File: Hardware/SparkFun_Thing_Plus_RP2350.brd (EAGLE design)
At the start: 22.9 x 58.4 mm, 161 parts, among them J1 THING_PLUS_LOGICAL, J3 QWIIC_RIGHT_ANGLE, J6 MICRO-SD-ATOM, Q1 100mA/20V/3.8Ω, U1 RP2350A, U2 RM2, U3 RT9080-33GJ5, U4 LM66200, U5 W25QXX128MBIT, U6 MCP73831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

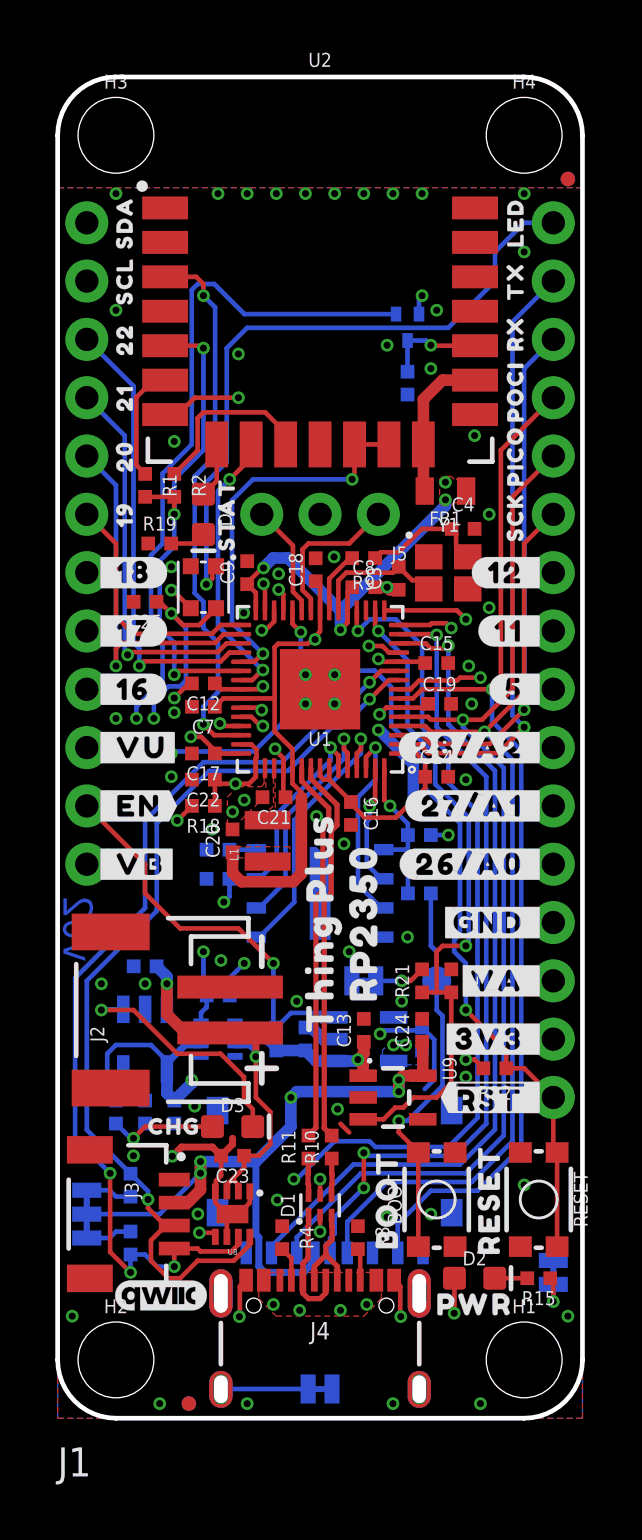
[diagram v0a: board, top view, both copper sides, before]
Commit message: Design review updates
Replace USB ESD diode with larger package for better manufacturing reliability
Add ordering instructions
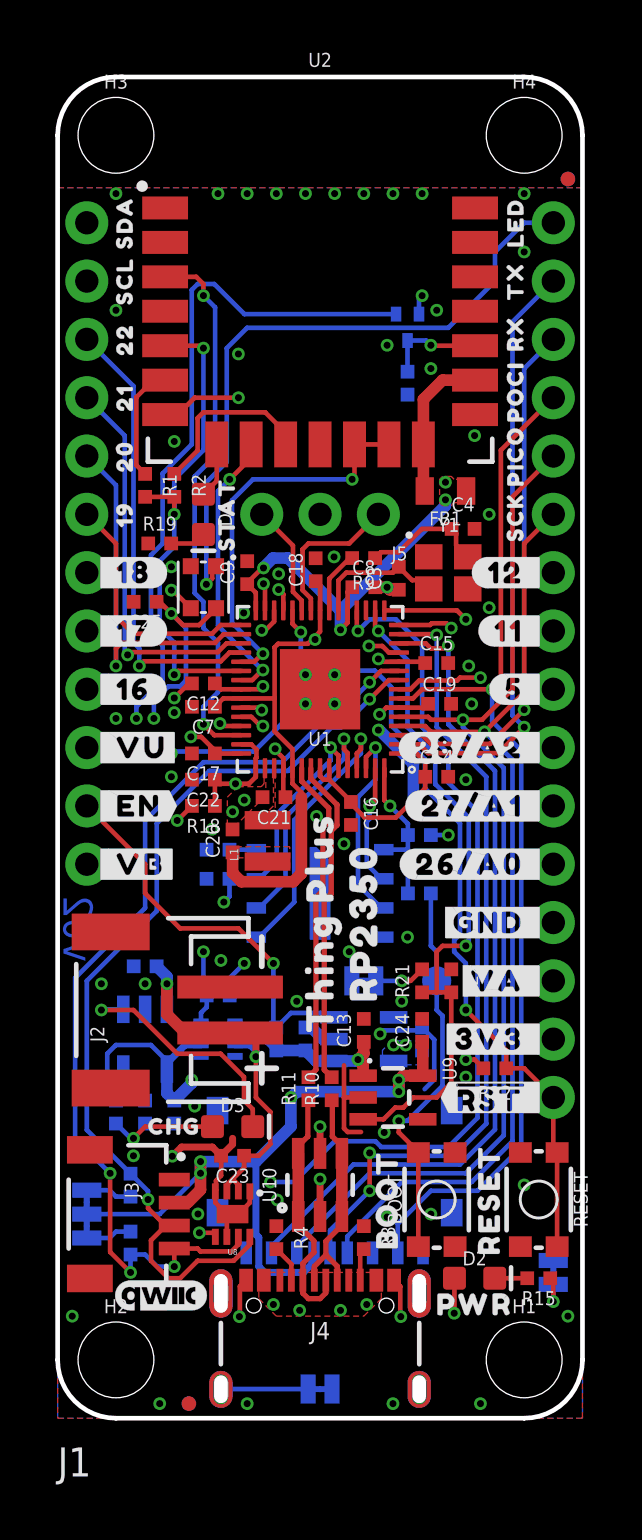
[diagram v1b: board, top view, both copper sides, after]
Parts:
- removed D1: PRTR5V0U2F, SparkFun-IC-Power:SOT886
- added LOGO5: SPECIAL_INSTRUCTIONS-ORDERING, SparkFun-Aesthetics:ORDERING_INSTRUCTIONS
- added U10: ESD Diode, SparkFun-DiscreteSemi:SOT-23-6
- moved FRAME1 14.0 mm to (66.0, -7.62)
- moved R10 2.54 mm to (11.9, 14.4)
- moved R11 2.54 mm to (10.9, 14.4)
- moved R3 0.25 mm to (13.3, 7.87)
- moved R4 0.25 mm to (9.53, 7.87)
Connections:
- removed net N$24: D1.4, R10.1
- removed net N$25: D1.6, R11.1
- net GND: now also U10.2; no longer D1.2
- net N$7: now also R11.1, U10.1, U10.6; no longer D1.1
- net N$8: now also R10.1, U10.3, U10.4; no longer D1.3
- net V_USB: now also U10.5; no longer D1.5
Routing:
- net N$7: track 5.28 -> 10.8 mm
- net N$8: track 4.47 -> 9.83 mm
- net GND: track 35.9 -> 40.7 mm
- net USB_D_P: track 16.8 -> 14.3 mm
- net USB_D_N: track 16.9 -> 14.3 mm
- net N$24: track 1.63 -> 0.00 mm
- net N$25: track 1.63 -> 0.00 mm
- net V_USB: track 48.2 -> 49.4 mm
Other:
- board text added: "4-layer JLC7628 Stackup Material: TG135-140 1oz outer layers 0.5oz inner layers Board thickness: 1.6mm Soldermask: Red Silkscreen: White Surface Finish: Lead-Free HASL"

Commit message: Add PSRAM
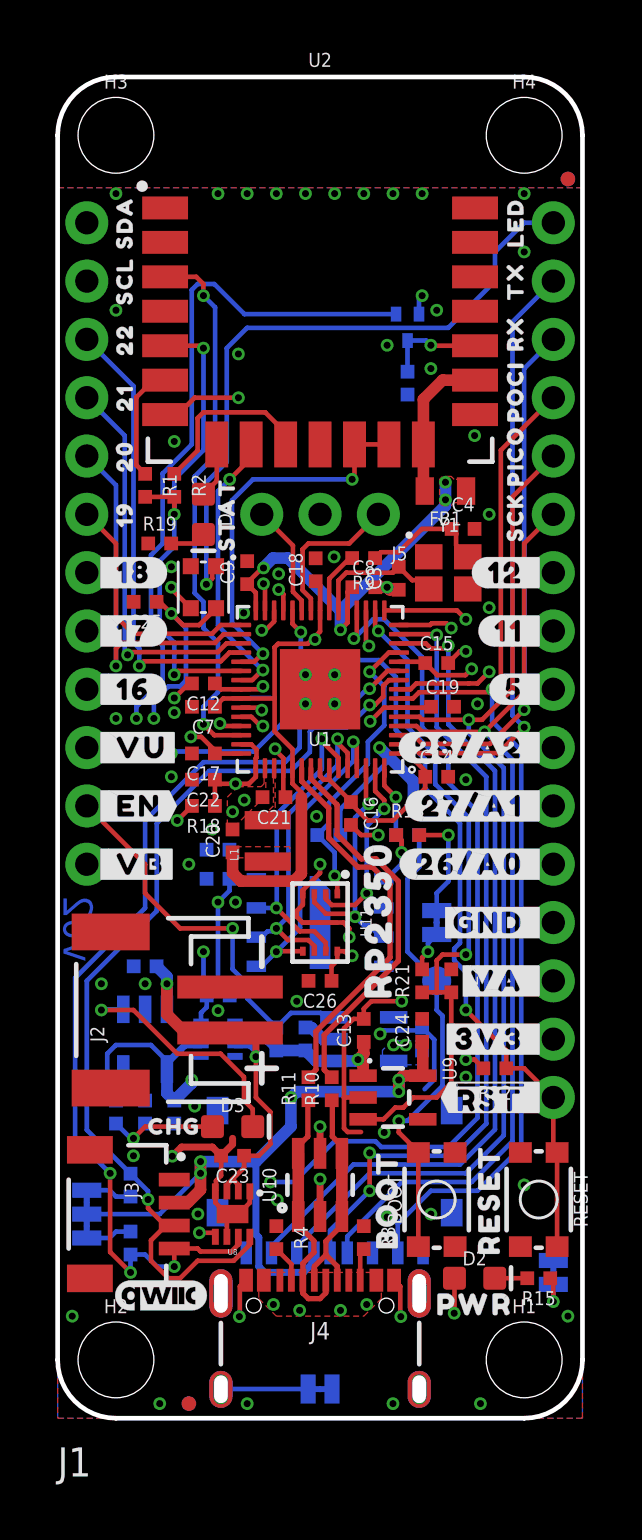
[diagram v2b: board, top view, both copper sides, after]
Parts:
- removed U$37: (no value), output:#_A0#26#0
- added C26: 0.1uF, SparkFun-Capacitors:0402-TIGHT
- added R23: 10k, SparkFun-Resistors:0402-TIGHT
- added U11: APS6404L-3SQR-ZR, RP2350A:APS6404L-3SQR-ZR
- U$16: device output:#_GND#0 -> output:#_A0#0
- U$44: device output:THING_PLUS0 -> output:#_G#0
- moved U$44 9.91 mm to (21.3, 21.6), flipped to the bottom, turned to 0 degrees
- moved U$26 5.32 mm to (16.5, 22.5), turned to 90 degrees
- moved LP 4.07 mm to (16.5, 21.6), turned to 90 degrees
- moved R14 2.59 mm to (15.2, 25.4)
- moved U$16 2.54 mm to (21.3, 24.1)
- moved C10 1.27 mm to (6.99, 24.8)
- moved C11 1.27 mm to (6.99, 23.5)
- moved U5 1.27 mm to (11.4, 21.6)
- moved U$45 0.65 mm to (14.0, 21.7)
- moved R13 0.51 mm to (15.2, 25.4), flipped to the top, turned to 0 degrees
- moved C19 0.18 mm to (16.8, 31.0)
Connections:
- new net PSRAM_!CS!: R23.1, U1.12, U11.1
- net 3.3V: now also C26.1, R23.2, U11.8
- net GND: now also C26.2, U11.4, U11.9
- net LED_IN: now also U1.18; no longer U1.12
- net QSPI_CLK: now also U11.6
- net QSPI_D0: now also U11.5
- net QSPI_D1: now also U11.2
- net QSPI_D2: now also U11.3
- net QSPI_D3: now also U11.7
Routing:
- net PSRAM_!CS!: track 0.00 -> 13.1 mm, vias 0 -> 2
- net 3.3V: track 50.1 -> 63.1 mm, vias 20 -> 19
- net GND: track 40.7 -> 53.4 mm, vias 69 -> 72
- net QSPI_D3: track 8.17 -> 13.8 mm, vias 1 -> 2
- net QSPI_D1: track 5.34 -> 9.27 mm, vias 1 -> 2
- net QSPI_CLK: track 10.4 -> 14.0 mm, vias 1 -> 2
- net !BOOT!: track 17.0 -> 20.1 mm
- net USB_D_P: track 14.3 -> 16.9 mm
- net USB_D_N: track 14.3 -> 16.9 mm
- net QSPI_D0: track 11.9 -> 14.0 mm, vias 1 -> 2
- net QSPI_D2: track 8.90 -> 10.8 mm, vias 1 -> 2
- net SDA: track 71.1 -> 72.2 mm
- net SCL: track 69.8 -> 70.6 mm
- net QSPI_!CS!: track 6.93 -> 6.39 mm, vias 1 -> 2

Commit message: Bump version number to v10
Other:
- board text added: "v10"
- board text removed: "v02"
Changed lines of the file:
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@@
 <wire x1="8.89" y1="20.955" x2="8.89" y2="19.685" width="0.254" layer="21"/>
 <wire x1="8.89" y1="15.875" x2="8.89" y2="14.605" width="0.254" layer="21"/>
-<text x="0.889" y="21.336" size="1.27" layer="16" font="vector" ratio="15" rot="MR270" align="center">v02</text>
+<text x="0.889" y="21.336" size="1.27" layer="16" font="vector" ratio="15" rot="MR270" align="center">v10</text>
 <text x="92.71" y="-7.62" size="1.778" layer="51" font="vector">Dryw Wade</text>
 <dimension x1="5.08" y1="8.89" x2="5.08" y2="0" x3="-1.27" y3="4.445" textsize="1.778" textratio="15" layer="47" unit="inch"/>
@@
 <element name="FRAME1" library="SparkFun-Aesthetics" package="CREATIVE_COMMONS" value="FRAME-LEDGER" x="66.04" y="-7.62" smashed="yes">
 <attribute name="DESIGNER" value="Dryw Wade" x="66.04" y="-7.62" size="1.778" layer="27" font="vector" ratio="15" display="off"/>
-<attribute name="REV" value="v02" x="66.04" y="-7.62" size="1.778" layer="27" font="vector" ratio="15" display="off"/>
+<attribute name="REV" value="v10" x="66.04" y="-7.62" size="1.778" layer="27" font="vector" ratio="15" display="off"/>
 </element>
 <element name="Y1" library="SparkFun-Clocks" package="CRYSTAL-SMD-2X2.5MM" value="12MHz" x="17.018" y="36.83" smashed="yes">

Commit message: Checklist review updates
Add "Based on design by:"
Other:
- board text added: "Based on design by: Nathan Seidle"
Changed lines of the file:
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@@
 Silkscreen: White
 Surface Finish: Lead-Free HASL</text>
+<text x="68.58" y="-10.16" size="1.778" layer="51" font="vector">Based on design by: Nathan Seidle</text>
 </plain>
 <attributes>

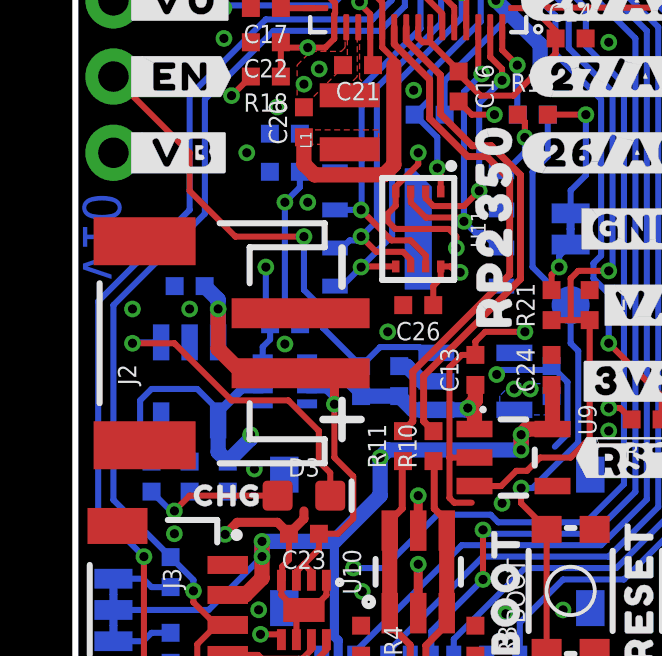
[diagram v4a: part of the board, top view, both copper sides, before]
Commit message: Fix battery polarity
Bump version number to v11
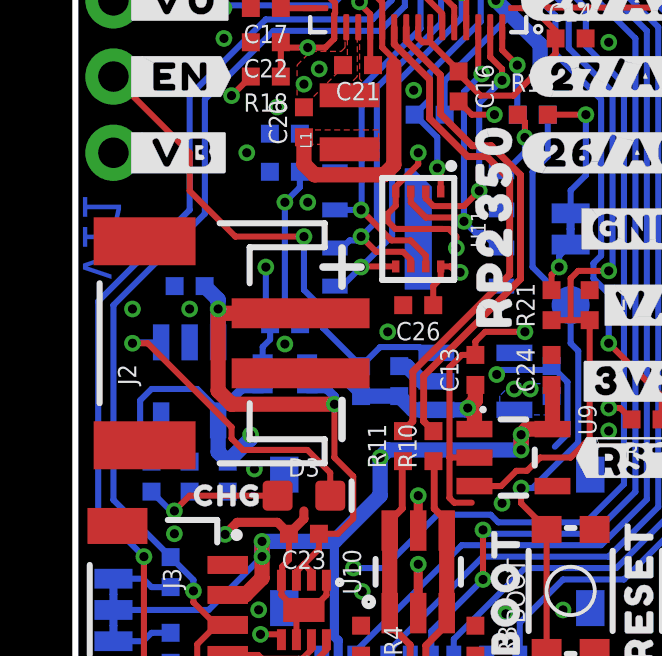
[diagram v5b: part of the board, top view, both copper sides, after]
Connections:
- net GND: now also J2.1; no longer J2.2
- net V_BATT: now also J2.2; no longer J2.1
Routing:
- net V_BATT: track 29.5 -> 32.7 mm
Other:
- board text added: "v11"
- board text removed: "v10"
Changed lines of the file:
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@@
 <wire x1="20.32" y1="58.42" x2="22.86" y2="55.88" width="0.2032" layer="20" curve="-90"/>
 <wire x1="0" y1="55.88" x2="2.54" y2="58.42" width="0.2032" layer="20" curve="-90"/>
-<wire x1="8.255" y1="15.24" x2="9.525" y2="15.24" width="0.254" layer="21"/>
+<wire x1="8.255" y1="20.32" x2="9.525" y2="20.32" width="0.254" layer="21"/>
 <wire x1="8.89" y1="20.955" x2="8.89" y2="19.685" width="0.254" layer="21"/>
 <wire x1="8.89" y1="15.875" x2="8.89" y2="14.605" width="0.254" layer="21"/>
-<text x="0.889" y="21.336" size="1.27" layer="16" font="vector" ratio="15" rot="MR270" align="center">v10</text>
+<text x="0.889" y="21.336" size="1.27" layer="16" font="vector" ratio="15" rot="MR270" align="center">v11</text>
 <text x="92.71" y="-7.62" size="1.778" layer="51" font="vector">Dryw Wade</text>
 <dimension x1="5.08" y1="8.89" x2="5.08" y2="0" x3="-1.27" y3="4.445" textsize="1.778" textratio="15" layer="47" unit="inch"/>
@@
 <element name="FRAME1" library="SparkFun-Aesthetics" package="CREATIVE_COMMONS" value="FRAME-LEDGER" x="66.04" y="-7.62" smashed="yes">
 <attribute name="DESIGNER" value="Dryw Wade" x="66.04" y="-7.62" size="1.778" layer="27" font="vector" ratio="15" display="off"/>
-<attribute name="REV" value="v10" x="66.04" y="-7.62" size="1.778" layer="27" font="vector" ratio="15" display="off"/>
+<attribute name="REV" value="v11" x="66.04" y="-7.62" size="1.778" layer="27" font="vector" ratio="15" display="off"/>
 </element>
 <element name="Y1" library="SparkFun-Clocks" package="CRYSTAL-SMD-2X2.5MM" value="12MHz" x="17.018" y="36.83" smashed="yes">
@@
 <contactref element="J1" pad="25"/>
 <contactref element="J3" pad="1"/>
-<contactref element="J2" pad="2"/>
 <contactref element="SHLD" pad="1"/>
 <contactref element="R3" pad="1"/>
@@
 <wire x1="12.4714" y1="16.9799" x2="12.4714" y2="13.97" width="0.2032" layer="1"/>
 <wire x1="9.271" y1="31.369" x2="8.382" y2="31.369" width="0.2032" layer="16"/>
+<contactref element="J2" pad="1"/>
 </signal>
 <signal name="V_USB">
@@
 <signal name="V_BATT">
 <contactref element="J1" pad="12"/>
-<contactref element="J2" pad="1"/>
 <contactref element="U4" pad="3"/>
 <contactref element="U6" pad="3"/>
@@
 <wire x1="8.636" y1="16.002" x2="8.636" y2="15.748" width="0.3048" layer="16"/>
 <via x="8.636" y="15.748" extent="1-16" drill="0.3048"/>
-<wire x1="8.636" y1="15.748" x2="8.636" y2="16.51" width="0.3048" layer="1"/>
-<wire x1="8.636" y1="16.51" x2="8.366" y2="16.78" width="0.3048" layer="1"/>
-<wire x1="8.366" y1="16.78" x2="7.51" y2="16.78" width="0.3048" layer="1"/>
 <wire x1="9.263" y1="13.343" x2="8.636" y2="13.97" width="0.2032" layer="1"/>
 <wire x1="8.636" y1="15.748" x2="8.636" y2="13.97" width="0.2032" layer="1"/>
@@
 <wire x1="4.76" y1="19.235" x2="4.76" y2="18.923" width="0.508" layer="16"/>
 <via x="4.76" y="18.923" extent="1-16" drill="0.3048"/>
-<wire x1="4.76" y1="18.923" x2="4.76" y2="17.592" width="0.508" layer="1"/>
-<wire x1="5.572" y1="16.78" x2="7.51" y2="16.78" width="0.508" layer="1"/>
-<wire x1="4.76" y1="17.592" x2="5.572" y2="16.78" width="0.508" layer="1"/>
+<wire x1="4.76" y1="18.923" x2="4.76" y2="16.195" width="0.508" layer="1"/>
 <wire x1="4.76" y1="18.923" x2="1.27" y2="22.413" width="0.508" layer="15"/>
 <wire x1="1.27" y1="24.13" x2="1.27" y2="22.413" width="0.508" layer="15"/>
 <wire x1="4.76" y1="18.923" x2="7.935" y2="15.748" width="0.508" layer="15"/>
 <wire x1="7.935" y1="15.748" x2="8.636" y2="15.748" width="0.508" layer="15"/>
+<contactref element="J2" pad="2"/>
+<wire x1="7.51" y1="18.78" x2="4.903" y2="18.78" width="0.508" layer="1"/>
+<wire x1="4.903" y1="18.78" x2="4.76" y2="18.923" width="0.508" layer="1"/>
+<wire x1="5.207" y1="15.748" x2="8.636" y2="15.748" width="0.508" layer="1"/>
+<wire x1="4.76" y1="16.195" x2="5.207" y2="15.748" width="0.508" layer="1"/>
 </signal>
 <signal name="SCL">
@@
 <contactref element="D3" pad="C"/>
 <contactref element="U6" pad="1"/>
-<wire x1="8.116" y1="14.859" x2="8.116" y2="13.843" width="0.2032" layer="1"/>
 <wire x1="8.497" y1="12.7" x2="8.497" y2="13.462" width="0.2032" layer="1"/>
-<wire x1="8.497" y1="13.462" x2="8.116" y2="13.843" width="0.2032" layer="1"/>
-<wire x1="8.116" y1="14.859" x2="7.1" y2="15.875" width="0.2032" layer="1"/>
-<wire x1="7.1" y1="15.875" x2="5.207" y2="15.875" width="0.2032" layer="1"/>
-<wire x1="5.207" y1="15.875" x2="3.302" y2="17.78" width="0.2032" layer="1"/>
-<wire x1="3.302" y1="17.78" x2="1.905" y2="17.78" width="0.2032" layer="1"/>
+<wire x1="8.497" y1="13.462" x2="7.735" y2="14.224" width="0.2032" layer="1"/>
+<wire x1="7.735" y1="14.224" x2="5.588" y2="14.224" width="0.2032" layer="1"/>
+<wire x1="5.207" y1="14.605" x2="5.588" y2="14.224" width="0.2032" layer="1"/>
 <via x="1.905" y="17.78" extent="1-16" drill="0.3048"/>
 <wire x1="2.86" y1="17.8101" x2="1.9351" y2="17.8101" width="0.2032" layer="16"/>
 <wire x1="1.9351" y1="17.8101" x2="1.905" y2="17.78" width="0.2032" layer="16"/>
+<wire x1="1.905" y1="17.78" x2="2.413" y2="17.78" width="0.2032" layer="1"/>
+<wire x1="5.207" y1="14.986" x2="5.207" y2="14.605" width="0.2032" layer="1"/>
+<wire x1="2.413" y1="17.78" x2="5.207" y2="14.986" width="0.2032" layer="1"/>
 </signal>
 <signal name="VDDA">
